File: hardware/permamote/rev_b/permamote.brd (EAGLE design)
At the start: 25 x 54.1 mm, 97 parts, among them J1 TC2030-JLINK-NL, J2 M10X2, J3 M04X2, J5 MICRO_USB_B_HIROSE_ZX62R-B-5P, Q1 PMDXB950UPEL, Q10 PMDXB950UPEL, Q2 PMDXB950UPEL, Q3 PMDXB950UPEL, Q4 PMDXB950UPEL, Q5 PMDXB950UPEL, Q6 PMDXB950UPEL, Q7 PMDXB950UPEL, Q8 PMDXB950UPEL, U1 AB1815-T3, U10 NRF52840, U11 SI7021-A20-GM1, U12 FT232RQ, U2 BQ25505, U3 EKMB1101111, U4 ISL29125, U5 LIS2DW12, U6 MAX17222, U7 MAX44009, U8 MS5637-02BA03, X1 32MHz, X3 32.768kHz, X4 ABS07-32.768KHZ-7-T

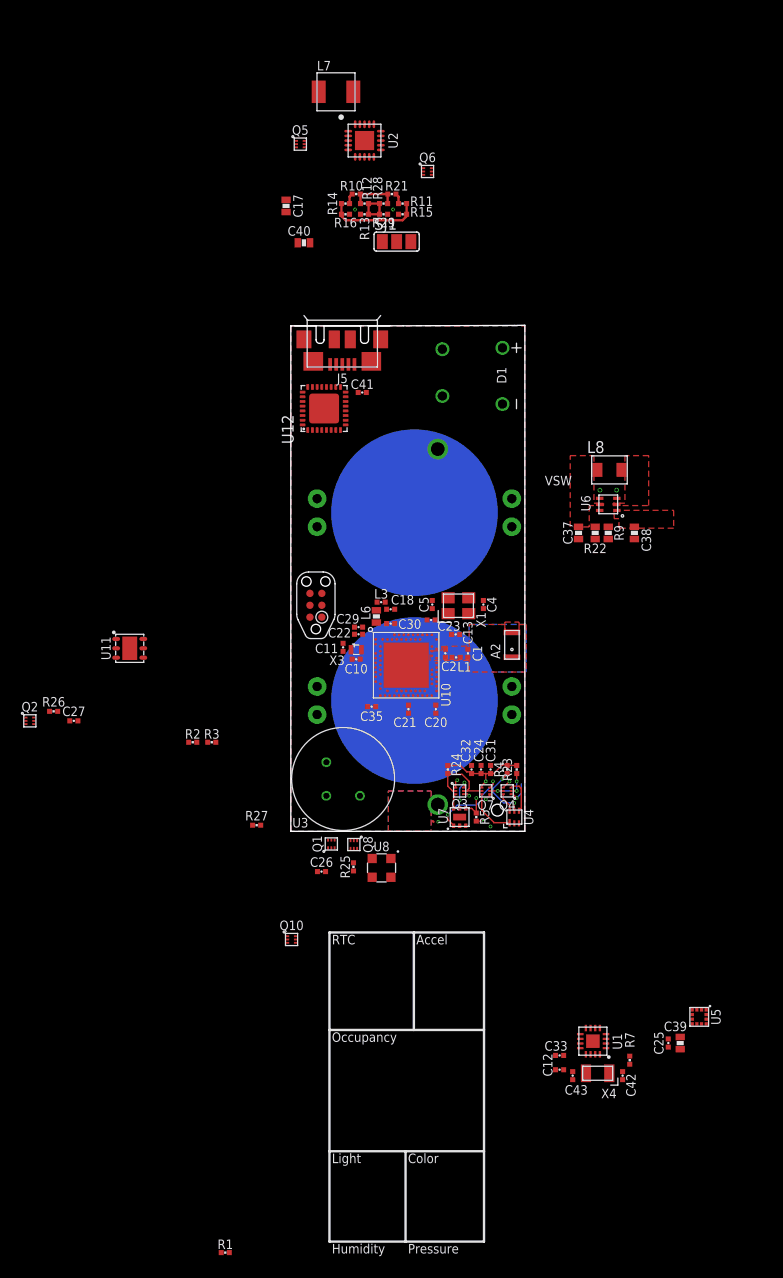
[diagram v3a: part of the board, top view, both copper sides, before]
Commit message: WIP
Finish power routing
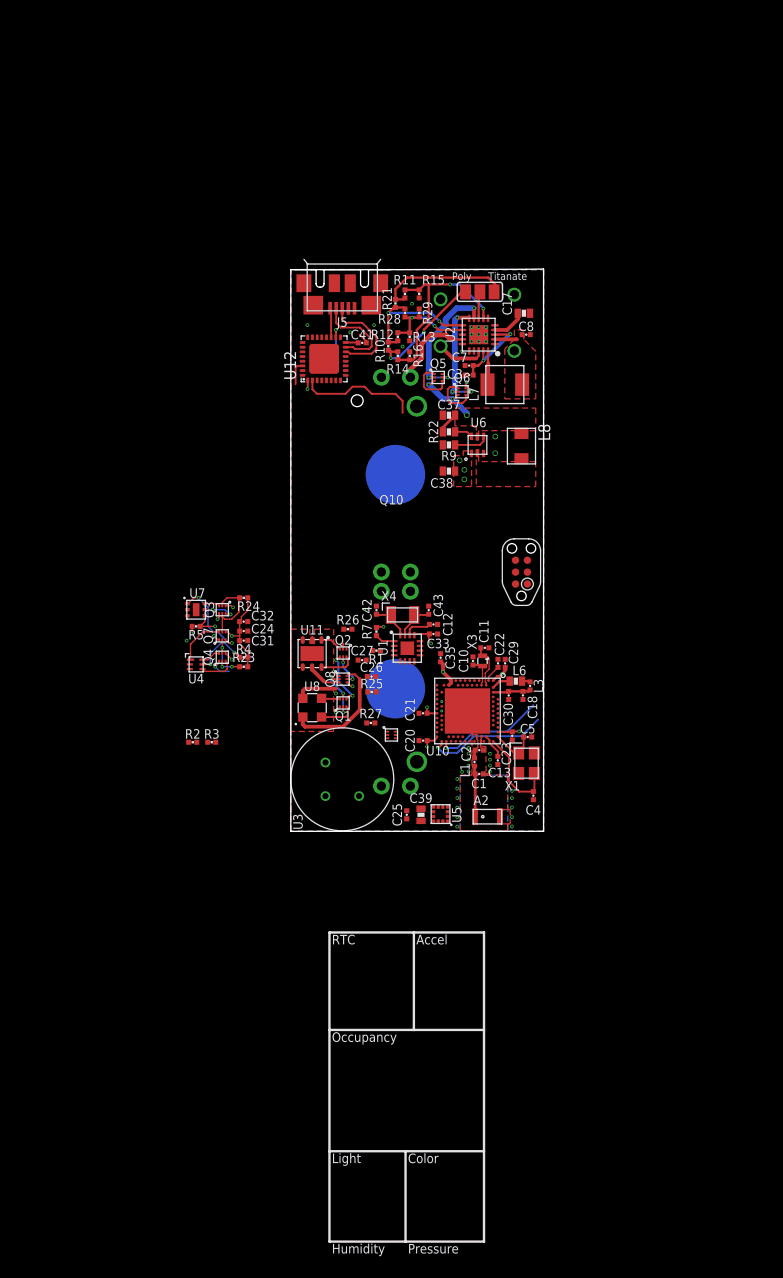
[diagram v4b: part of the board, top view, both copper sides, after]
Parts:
- removed C40: 4.7uF, passives:0603_CAP
- added C3: 0.01uF, passives:0402_CAP
- added C7, C8: 4.7uF, passives:0402_CAP
- BT2, BT3: value BAT-HLD-20XX-THRU -> BAT-HLD-002-THM; device batteries:BAT-HLD-20XX-THRU -> batteries:BAT-HLD-002-THM
- moved R1 66.3 mm to (9.14, 19.3), turned to 180 degrees
- moved C42 56.2 mm to (9.14, 23.6), turned to 90 degrees
- moved X4 53.2 mm to (11.9, 23.1), turned to 0 degrees
- moved R7 53.2 mm to (9.14, 21.3), turned to 90 degrees
- moved C43 52.0 mm to (14.7, 23.6), turned to 90 degrees
- moved C12 49.4 mm to (15.2, 22.1), turned to 0 degrees
- moved C33 47.0 mm to (15.2, 21.1), turned to 0 degrees
- moved U1 46.4 mm to (12.4, 19.6), turned to 0 degrees
- moved U4 37.7 mm to (-10.1, 17.8), turned to 0 degrees
- moved C25 37.1 mm to (12.4, 1.77)
- moved C39 36.9 mm to (13.9, 1.77)
- moved R5 36.2 mm to (-10.1, 21.9), turned to 180 degrees
- moved L7 36.1 mm to (22.9, 47.7), turned to 180 degrees
- moved U7 35.8 mm to (-10.1, 23.7), turned to 0 degrees
- moved U5 35.1 mm to (16.0, 1.84), turned to 180 degrees
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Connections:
- net N$30 renamed VREF_SAMP
- net N$40 renamed LBST
- net N$46 renamed !VBAT_SEC_ON
- net N$56 renamed !VBAT_PRI_ON
- removed net N$47: Q5.6, U2.19, U2.3
- new net VOC_SAMP_VSTOR: C3.1, C7.1, Q5.6, U2.19, U2.3
- net GND: now also C3.2, C7.2, C8.2; no longer C40.2
- net VBAT: now also BT2.POS1, BT2.POS2, BT2.POS3, BT2.POS4, BT3.POS1, BT3.POS2, BT3.POS3, BT3.POS4; no longer BT2.+1, BT2.+2, BT2.+3, BT2.+4, BT3.+1, BT3.+2, BT3.+3, BT3.+4
- net VSOL: now also C8.1; no longer C40.1
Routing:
- net VCC: track 11.3 -> 28.3 mm, vias 3 -> 16
- net !VBAT_SEC_ON: track 0.00 -> 14.8 mm, vias 0 -> 3
- net N$1: track 1.13 -> 14.5 mm
- net SWDIO: track 0.00 -> 13.2 mm, vias 0 -> 1
- net DBG_TX: track 0.00 -> 13.0 mm
- net N$21: track 0.00 -> 12.7 mm
- net !VBAT_PRI_ON: track 0.00 -> 12.5 mm, vias 0 -> 3
- net SWDCLK: track 0.00 -> 12.1 mm, vias 0 -> 1
- net N$16: track 1.13 -> 12.9 mm, vias 0 -> 2
- net N$18: track 10.0 -> 21.2 mm, vias 0 -> 2
- net D+: track 0.00 -> 10.5 mm
- net N$8: track 0.00 -> 10.0 mm
- net N$58: track 4.98 -> 14.8 mm, vias 0 -> 2
- net VBAT: track 0.00 -> 9.83 mm, vias 0 -> 1
- net D-: track 0.00 -> 9.81 mm
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- added copper zone on layer 2, net VBAT
- added copper zone on layer 1, net VSOL
- removed copper zone on layer 15, net N$10
- removed copper zone on layer 16, net N$10
- removed copper zone on layer 2, net N$10
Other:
- board size 25 x 54.1 mm -> 27 x 60.1 mm
- board text added: "Poly"
- board text added: "Titanate"
- board text removed: "VSW"
